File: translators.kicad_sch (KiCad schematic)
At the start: 34 parts

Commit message: [#52835] schematics: assign new netclasses
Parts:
- R10, R17, R18, R19, R21, R22, R23, R24, R3, R4, R5, R7, R8, R9: footprint antmicro-footprints:R_Array_4x0402 -> antmicro-footprints:R_Array_4x0402_Panasonic_EXB28V
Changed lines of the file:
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@@
       (effects (font (size 1.27 1.27) (thickness 0.15)) (justify left bottom) hide)
     )
-    (property "Footprint" "antmicro-footprints:R_Array_4x0402" (id 2) (at 287.02 125.73 0)
+    (property "Footprint" "antmicro-footprints:R_Array_4x0402_Panasonic_EXB28V" (id 2) (at 287.02 125.73 0)
       (effects (font (size 1.27 1.27) (thickness 0.15)) (justify left bottom) hide)
     )
@@
       (effects (font (size 1.27 1.27) (thickness 0.15)) (justify left bottom) hide)
     )
-    (property "Footprint" "antmicro-footprints:R_Array_4x0402" (id 2) (at 287.02 41.91 0)
+    (property "Footprint" "antmicro-footprints:R_Array_4x0402_Panasonic_EXB28V" (id 2) (at 287.02 41.91 0)
       (effects (font (size 1.27 1.27) (thickness 0.15)) (justify left bottom) hide)
     )
@@
       (effects (font (size 1.27 1.27) (thickness 0.15)) (justify left bottom) hide)
     )
-    (property "Footprint" "antmicro-footprints:R_Array_4x0402" (id 2) (at 287.02 55.88 0)
+    (property "Footprint" "antmicro-footprints:R_Array_4x0402_Panasonic_EXB28V" (id 2) (at 287.02 55.88 0)
       (effects (font (size 1.27 1.27) (thickness 0.15)) (justify left bottom) hide)
     )
@@
       (effects (font (size 1.27 1.27) (thickness 0.15)) (justify left bottom) hide)
     )
-    (property "Footprint" "antmicro-footprints:R_Array_4x0402" (id 2) (at 287.02 139.7 0)
+    (property "Footprint" "antmicro-footprints:R_Array_4x0402_Panasonic_EXB28V" (id 2) (at 287.02 139.7 0)
       (effects (font (size 1.27 1.27) (thickness 0.15)) (justify left bottom) hide)
     )
@@
       (effects (font (size 1.27 1.27) (thickness 0.15)) (justify left bottom) hide)
     )
-    (property "Footprint" "antmicro-footprints:R_Array_4x0402" (id 2) (at 287.02 97.79 0)
+    (property "Footprint" "antmicro-footprints:R_Array_4x0402_Panasonic_EXB28V" (id 2) (at 287.02 97.79 0)
       (effects (font (size 1.27 1.27) (thickness 0.15)) (justify left bottom) hide)
     )
@@
       (effects (font (size 1.27 1.27) (thickness 0.15)) (justify left bottom) hide)
     )
-    (property "Footprint" "antmicro-footprints:R_Array_4x0402" (id 2) (at 205.74 139.7 0)
+    (property "Footprint" "antmicro-footprints:R_Array_4x0402_Panasonic_EXB28V" (id 2) (at 205.74 139.7 0)
       (effects (font (size 1.27 1.27) (thickness 0.15)) (justify left bottom) hide)
     )
@@
       (effects (font (size 1.27 1.27) (thickness 0.15)) (justify left bottom) hide)
     )
-    (property "Footprint" "antmicro-footprints:R_Array_4x0402" (id 2) (at 205.74 111.76 0)
+    (property "Footprint" "antmicro-footprints:R_Array_4x0402_Panasonic_EXB28V" (id 2) (at 205.74 111.76 0)
       (effects (font (size 1.27 1.27) (thickness 0.15)) (justify left bottom) hide)
     )
@@
       (effects (font (size 1.27 1.27) (thickness 0.15)) (justify left bottom) hide)
     )
-    (property "Footprint" "antmicro-footprints:R_Array_4x0402" (id 2) (at 205.74 125.73 0)
+    (property "Footprint" "antmicro-footprints:R_Array_4x0402_Panasonic_EXB28V" (id 2) (at 205.74 125.73 0)
       (effects (font (size 1.27 1.27) (thickness 0.15)) (justify left bottom) hide)
     )
@@
       (effects (font (size 1.27 1.27) (thickness 0.15)) (justify left bottom) hide)
     )
-    (property "Footprint" "antmicro-footprints:R_Array_4x0402" (id 2) (at 205.74 41.91 0)
+    (property "Footprint" "antmicro-footprints:R_Array_4x0402_Panasonic_EXB28V" (id 2) (at 205.74 41.91 0)
       (effects (font (size 1.27 1.27) (thickness 0.15)) (justify left bottom) hide)
     )
@@
       (effects (font (size 1.27 1.27) (thickness 0.15)) (justify left bottom) hide)
     )
-    (property "Footprint" "antmicro-footprints:R_Array_4x0402" (id 2) (at 205.74 97.79 0)
+    (property "Footprint" "antmicro-footprints:R_Array_4x0402_Panasonic_EXB28V" (id 2) (at 205.74 97.79 0)
       (effects (font (size 1.27 1.27) (thickness 0.15)) (justify left bottom) hide)
     )
@@
       (effects (font (size 1.27 1.27) (thickness 0.15)) (justify left bottom) hide)
     )
-    (property "Footprint" "antmicro-footprints:R_Array_4x0402" (id 2) (at 205.74 69.85 0)
+    (property "Footprint" "antmicro-footprints:R_Array_4x0402_Panasonic_EXB28V" (id 2) (at 205.74 69.85 0)
       (effects (font (size 1.27 1.27) (thickness 0.15)) (justify left bottom) hide)
     )
@@
       (effects (font (size 1.27 1.27) (thickness 0.15)) (justify left bottom) hide)
     )
-    (property "Footprint" "antmicro-footprints:R_Array_4x0402" (id 2) (at 287.02 111.76 0)
+    (property "Footprint" "antmicro-footprints:R_Array_4x0402_Panasonic_EXB28V" (id 2) (at 287.02 111.76 0)
       (effects (font (size 1.27 1.27) (thickness 0.15)) (justify left bottom) hide)
     )
@@
       (effects (font (size 1.27 1.27) (thickness 0.15)) (justify left bottom) hide)
     )
-    (property "Footprint" "antmicro-footprints:R_Array_4x0402" (id 2) (at 205.74 55.88 0)
+    (property "Footprint" "antmicro-footprints:R_Array_4x0402_Panasonic_EXB28V" (id 2) (at 205.74 55.88 0)
       (effects (font (size 1.27 1.27) (thickness 0.15)) (justify left bottom) hide)
     )
@@
       (effects (font (size 1.27 1.27) (thickness 0.15)) (justify left bottom) hide)
     )
-    (property "Footprint" "antmicro-footprints:R_Array_4x0402" (id 2) (at 287.02 69.85 0)
-      (effects (font (size 1.27 1.27) (thickness 0.15)) (justify left bottom) hide)
-    )
+    (property "Footprint" "antmicro-footprints:R_Array_4x0402_Panasonic_EXB28V" (id 2) (at 287.02 69.85 0)
+      (effects (font (size 1.27 1.27) (thickness 0.15)) (justify left bottom) hide)
+    )

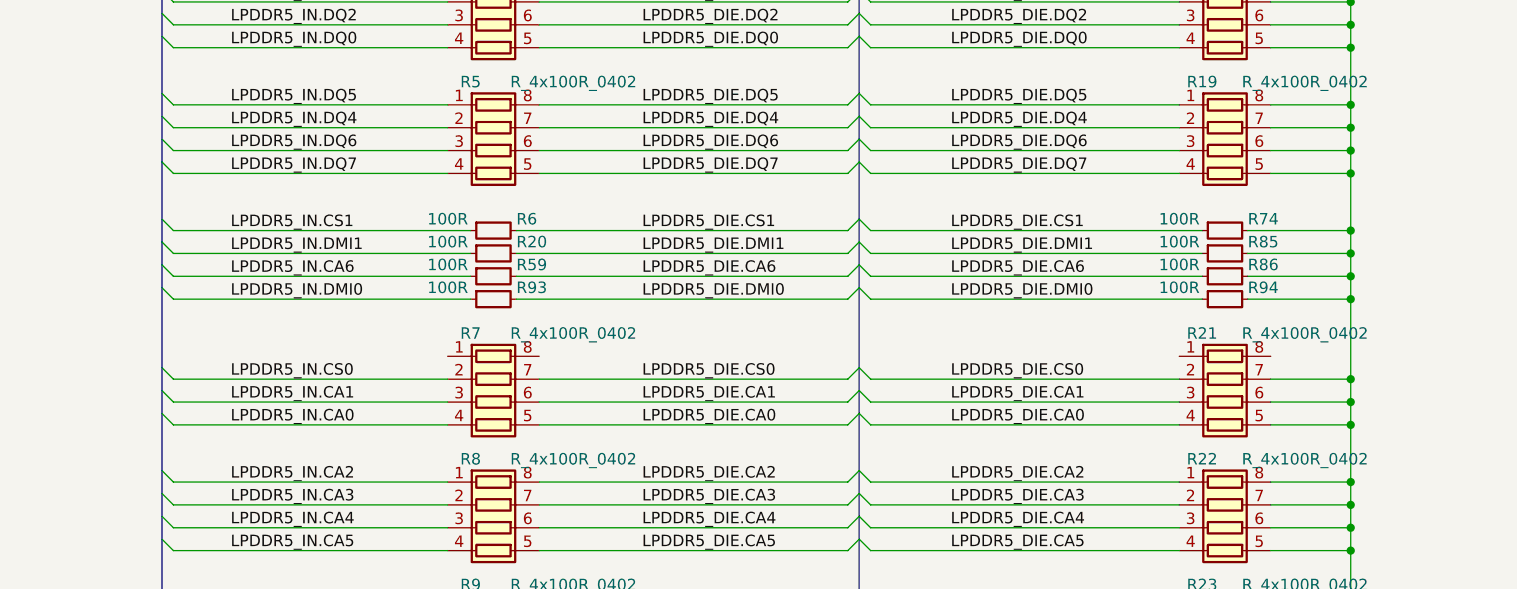
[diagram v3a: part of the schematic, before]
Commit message: [#52974] schematics: final connection of the A side of the die
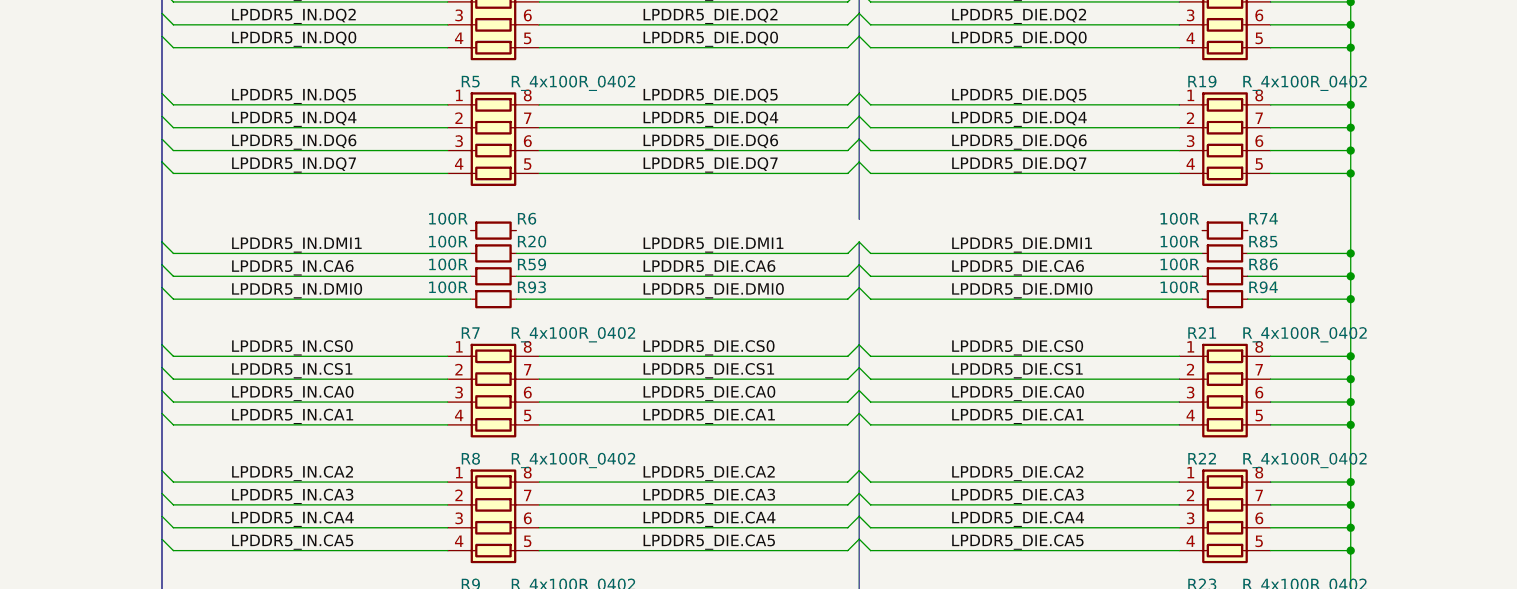
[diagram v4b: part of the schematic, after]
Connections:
- net GND: now also R21.8 (R1.2); no longer R74.2
- net LPDDR5_DIE.CA0: now also R21.3 (R3.1), R7.6 (R3.2); no longer R21.4 (R4.1), R7.5 (R4.2)
- net LPDDR5_DIE.CA1: now also R21.4 (R4.1), R7.5 (R4.2); no longer R21.3 (R3.1), R7.6 (R3.2)
- net LPDDR5_DIE.CS0: now also R21.1 (R1.1), R7.8 (R1.2); no longer R21.2 (R2.1), R7.7 (R2.2)
- net LPDDR5_DIE.CS1: now also R21.2 (R2.1), R7.7 (R2.2); no longer R6.2, R74.1
- net LPDDR5_IN.CA0: now also R7.3 (R3.1); no longer R7.4 (R4.1)
- net LPDDR5_IN.CA1: now also R7.4 (R4.1); no longer R7.3 (R3.1)
- net LPDDR5_IN.CS0: now also R7.1 (R1.1); no longer R7.2 (R2.1)
- net LPDDR5_IN.CS1: now also R7.2 (R2.1); no longer R6.1

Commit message: [#52835] update project name
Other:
- title: LPDDR5 SO-DIMM -> LPDDR5 Testbed
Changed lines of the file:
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@@
   (paper "A3")
   (title_block
-    (title "LPDDR5 SO-DIMM")
+    (title "LPDDR5 Testbed")
     (date "2023-12-19")
     (rev "1.0.0")

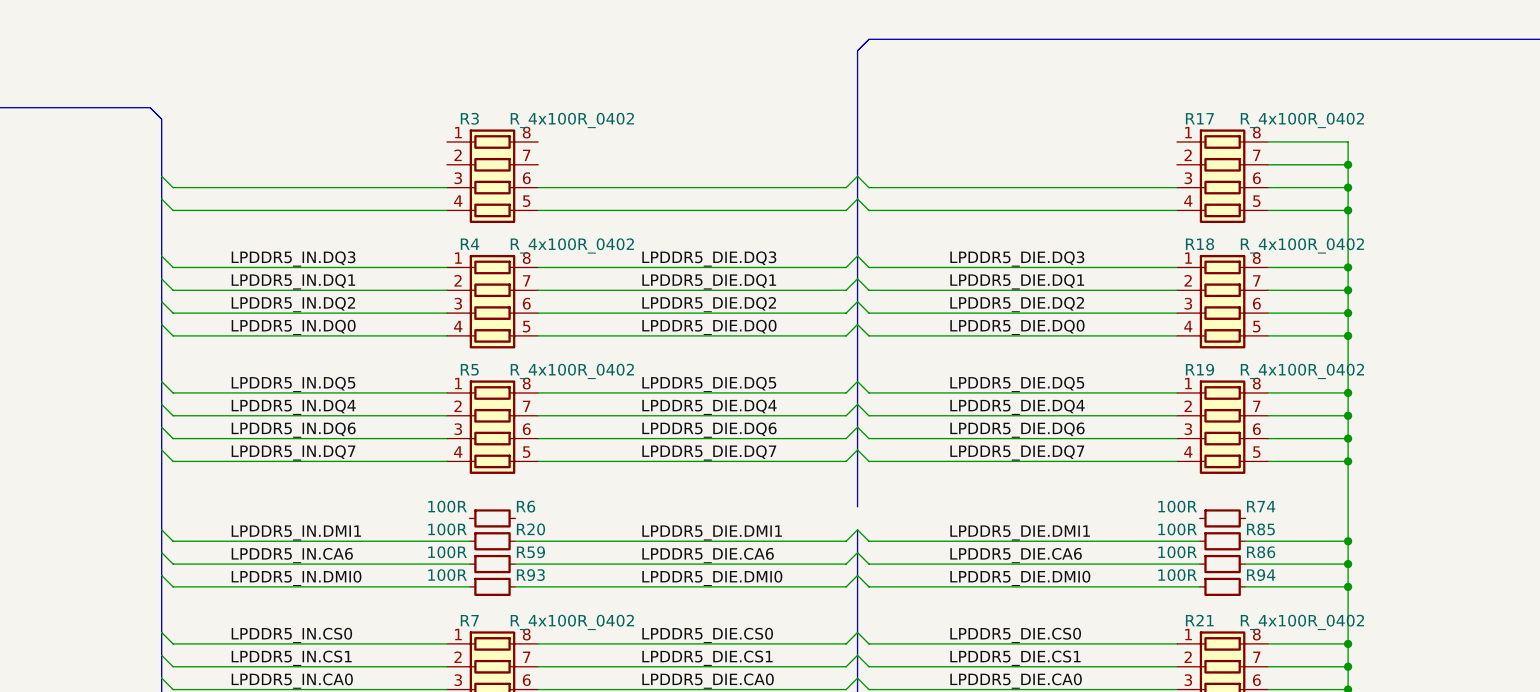
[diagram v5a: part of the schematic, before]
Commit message: [#52835] schematics: remove unnecessary resistors
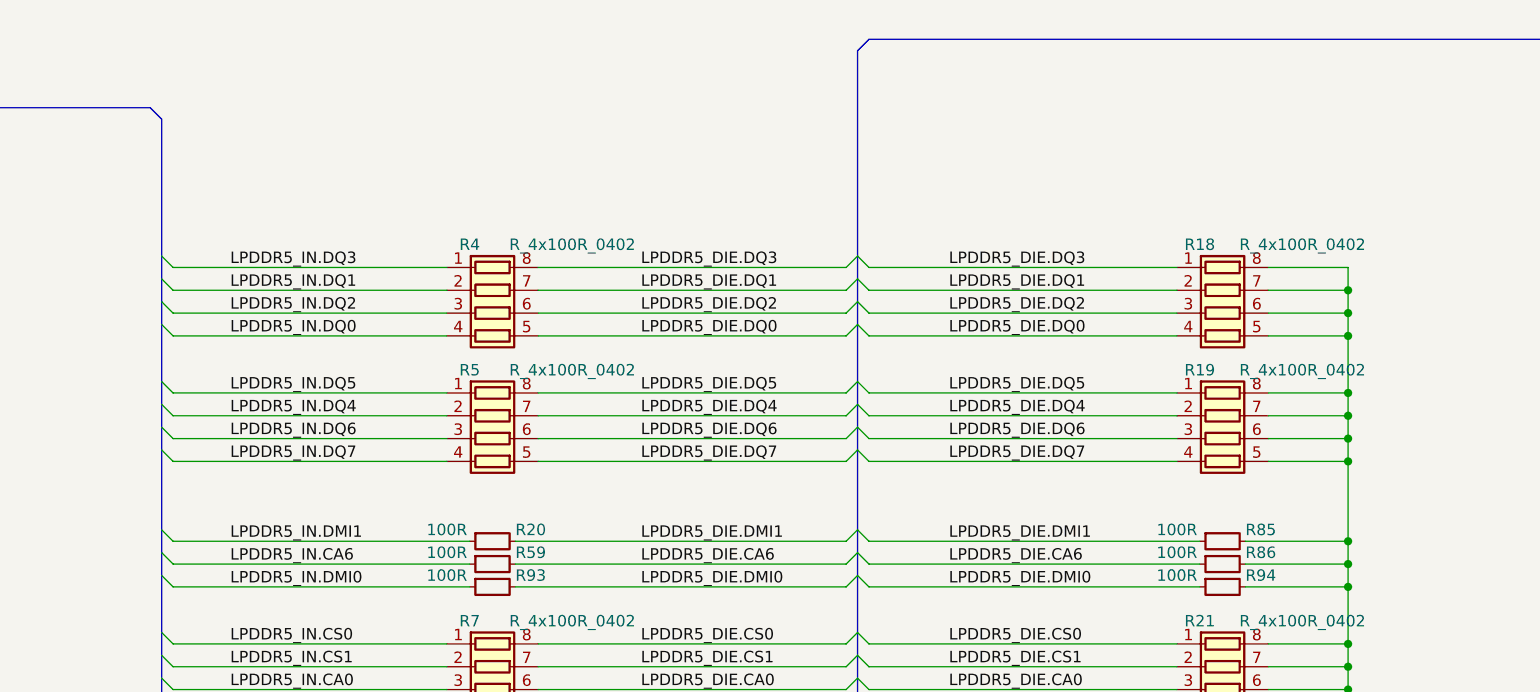
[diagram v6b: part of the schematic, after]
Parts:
- removed R17, R3: R_4x100R_0402_array, antmicro-footprints:R_Array_4x0402_Panasonic_EXB28V, symbol antmicroResistorNetworksArrays:R_4x100R_0402_array
- removed R6, R74: R_100R_0402, antmicro-footprints:R_0402_1005Metric, symbol antmicroResistors0402:R_100R_0402

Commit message: Loclib
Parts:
- R10, R18, R19, R21, R22, R23, R24, R4, R5, R7, R8, R9: footprint antmicro-footprints:R_Array_4x0402_Panasonic_EXB28V -> lpddr5-testbed-footprints:R_Array_4x0402_Panasonic_EXB28V; symbol antmicroResistorNetworksArrays:R_4x100R_0402_array -> lpddr5-testbed:R_4x100R_0402_array
- R11, R12, R13, R14, R15, R16, R20, R25, R48, R49, R53, R54, R55, R59, R85, R86, R93, R94: footprint antmicro-footprints:R_0402_1005Metric -> lpddr5-testbed-footprints:R_0402_1005Metric; symbol antmicroResistors0402:R_100R_0402 -> lpddr5-testbed:R_100R_0402
